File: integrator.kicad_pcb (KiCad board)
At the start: 2 copper layers, 60 x 72 mm, 13 parts, among them J1 SJ-3524-SMT, J2 SJ-3524-SMT, SW1 EVQP40B3M, SW2 EVQP40B3M, U1 Teensy3.2, U2 FXOS8700CQ

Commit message: snapshot everything for safety
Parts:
- added C4: 4.7uf, Capacitor_SMD:CP_Elec_5x4.5, B.Cu at (36.0, 129.9)
- added C5: 0.1uf, Capacitor_SMD:C_0805_2012Metric, B.Cu at (57.6, 26.8)
- added C6: 4.7uf, Capacitor_SMD:CP_Elec_5x4.5, B.Cu at (83.5, 129.9)
- added D1: SD0805S020S1R0, Diode_SMD:D_0805_2012Metric, B.Cu at (49.9, 36.4)
- added R2: 4.7k, Resistor_SMD:R_0805_2012Metric, B.Cu at (49.3, 117.3)
- added R3: 4.7k, Resistor_SMD:R_0805_2012Metric, B.Cu at (49.3, 112.2)
- added R4: 5k, Resistor_SMD:R_0805_2012Metric, B.Cu at (37.2, 32.8)
- added R5: 5k, Resistor_SMD:R_0805_2012Metric, B.Cu at (80.7, 32.8)
- added R6: 4.7k, Resistor_SMD:R_0805_2012Metric, B.Cu at (69.8, 36.6)
- added REF**: hackzone, export:hackzone, B.Cu at (59.7, 82.7)
- C1: value 0.1uF -> 10nf; footprint Capacitor_SMD:C_0603_1608Metric -> Capacitor_SMD:C_0805_2012Metric; moved to B.Cu
- C2: value 0.1uF -> 0.1uf; footprint Capacitor_SMD:C_0603_1608Metric -> Capacitor_SMD:C_0805_2012Metric; moved to B.Cu
- C3: value 0.1uF -> 2.2uf; footprint Capacitor_SMD:C_0603_1608Metric -> Capacitor_SMD:C_0805_2012Metric; moved to B.Cu
- J1, J2: moved to B.Cu
- LED1, LED2: footprint LED_SMD:LED_0603_1608Metric -> LED_SMD:LED_0805_2012Metric; moved to B.Cu
- POGO1: value Conn_02x06_Odd_Even_MountingPin -> PO pogos; footprint Connector_PinSocket_2.54mm:PinSocket_2x06_P2.54mm_Vertical -> export:813-22-012-30-004101-millmax-pogopins-2x6
- R1: footprint Resistor_SMD:R_0603_1608Metric -> Resistor_SMD:R_0805_2012Metric; moved to B.Cu
- SW1: footprint eec:Panasonic-EVQP40B3M-MFG-2pad -> Button_Switch_THT:TL1105VF100Q; moved to B.Cu
- SW2: footprint eec:Panasonic-EVQP40B3M-MFG-2pad -> export:TL1105VF100Q; moved to B.Cu
- U2: value FXOS8700CQ -> ICM-20600; footprint misc:FSOS8700CQ_PKG -> PQFN50P250X300X97-14N; moved to B.Cu
- moved U1 122.8 mm to (59.8, 117.2), turned to 90 degrees
- moved SW1 122.6 mm to (85.5, 47.9), turned to 270 degrees
- moved LED2 119.0 mm to (69.6, 20.0), turned to 0 degrees
- moved J2 116.9 mm to (83.2, 24.6)
- moved R1 116.7 mm to (60.2, 19.9), turned to 90 degrees
- moved J1 115.8 mm to (36.3, 24.6)
- moved LED1 115.1 mm to (50.0, 20.0), turned to 180 degrees
- moved SW2 112.8 mm to (34.0, 47.8), turned to 90 degrees
- moved U2 110.2 mm to (60.2, 23.9), turned to 270 degrees
- moved POGO1 109.4 mm to (59.7, 36.5), turned to 180 degrees
- moved C3 108.2 mm to (63.9, 26.7), turned to 0 degrees
- moved C2 106.0 mm to (63.9, 29.0)
- moved C1 104.9 mm to (63.9, 23.2), turned to 180 degrees
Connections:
- C1 pad 1: Net-(C1-Pad1) -> Earth
- C1 pad 2: Earth -> Net-(C1-Pad2)
- C2 pad 1: Net-(C2-Pad1) -> Net-(C1-Pad2)
- C3 pad 1: Net-(C3-Pad1) -> Net-(C1-Pad2)
- J1 pad 1: Earth -> Net-(J1-Pad1)
- J2 pad 1: Earth -> Net-(J1-Pad1)
- POGO1 pad 4: Net-(POGO1-Pad4) -> Net-(D1-Pad2)
- SW2 pad 1: Earth -> Net-(SW2-Pad1)
- SW2 pad 2: Net-(SW2-Pad2) -> Earth
- U1 pad 11: Net-(SW2-Pad2) -> Net-(SW2-Pad1)
- U1 pad 13: Net-(U1-Pad13) -> Net-(J1-Pad2)
- U1 pad 16: Net-(C1-Pad1) -> Net-(U1-Pad16)
- U1 pad 19: Net-(J2-Pad3) -> Net-(R4-Pad1)
- U1 pad 25: Net-(U1-Pad25) -> Net-(R3-Pad2)
- U1 pad 26: Net-(U1-Pad26) -> Net-(R2-Pad2)
- U1 pad 31: Net-(U1-Pad31) -> Net-(C1-Pad2)
- U1 pad 32: Net-(U1-Pad32) -> Net-(J1-Pad1)
- U1 pad 33: Net-(POGO1-Pad4) -> Net-(U1-Pad33)
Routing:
- net Net-(C1-Pad2): track 0.00 -> 290.7 mm, vias 0 -> 8
- net Net-(J1-Pad1): track 0.00 -> 142.1 mm, vias 0 -> 2
- net (no net): track 0.00 -> 124.5 mm
- net Net-(POGO1-Pad4): track 86.2 -> 0.00 mm, vias 1 -> 0
- net Net-(R4-Pad1): track 0.00 -> 85.7 mm, vias 0 -> 2
- net Net-(POGO1-Pad5): track 85.5 -> 0.00 mm, vias 1 -> 0
- net Net-(POGO1-Pad7): track 82.5 -> 0.00 mm, vias 1 -> 0
- net Net-(POGO1-Pad9): track 79.7 -> 0.00 mm, vias 1 -> 0
- net Net-(J2-Pad3): track 94.3 -> 16.8 mm, vias 3 -> 0
- net Net-(J1-Pad2): track 0.00 -> 76.8 mm, vias 0 -> 1
- net Net-(POGO1-Pad12): track 106.1 -> 34.9 mm, vias 3 -> 0
- net Net-(POGO1-Pad3): track 85.4 -> 19.5 mm, vias 0 -> 2
- net Earth: track 97.6 -> 34.2 mm, vias 6 -> 16
- net Net-(J2-Pad2): track 92.8 -> 47.5 mm, vias 2 -> 1
- net Net-(U1-Pad4): track 44.0 -> 3.34 mm, vias 2 -> 1
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- added copper zone on In1.Cu, net Earth
- added copper zone on In2.Cu, net Earth
- added copper zone on In1.Cu, net Net-(J1-Pad1)
- removed copper zone on F.Cu, net Earth
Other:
- board size 60 x 72 mm -> 65.5 x 217 mm
- copper layers 2 -> 4
- net class +3.3v removed
- net class +v supply added: clearance 0.1524, trace_width 0.5, via_dia 0.6858, via_drill 0.3302
- net class audio added: clearance 0.1524, trace_width 0.5, via_dia 0.6858, via_drill 0.3302
- rule trace_min: 0.1524 -> 0.127

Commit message: snapshot with hackzone
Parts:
- moved D1 72.1 mm to (46.0, 108.3)
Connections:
- U1 pad 2: Net-(U1-Pad2) -> Net-(SW1-Pad2)
- U1 pad 5: Net-(SW1-Pad2) -> Net-(U1-Pad5)
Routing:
- net Net-(J1-Pad1): track 142.1 -> 312.8 mm
- net Net-(R3-Pad2): track 11.5 -> 121.7 mm
- net Net-(POGO1-Pad6): track 54.7 -> 160.0 mm
- net Net-(U1-Pad3): track 4.66 -> 105.9 mm, vias 1 -> 0
- net Net-(POGO1-Pad5): track 0.00 -> 95.7 mm
- net Net-(LED2-Pad2): track 67.3 -> 155.7 mm
- net Net-(D1-Pad2): track 9.50 -> 96.5 mm, vias 0 -> 2
- net Net-(R2-Pad2): track 11.8 -> 93.0 mm
- net Net-(SW1-Pad2): track 20.1 -> 90.4 mm
- net Net-(LED1-Pad2): track 68.3 -> 130.3 mm
- net Net-(POGO1-Pad12): track 34.9 -> 96.4 mm
- net Net-(U1-Pad4): track 3.34 -> 60.9 mm, vias 1 -> 0
- net Net-(R4-Pad1): track 85.7 -> 142.1 mm
- net Net-(POGO1-Pad9): track 0.00 -> 54.0 mm
- net Net-(POGO1-Pad7): track 0.00 -> 52.2 mm
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
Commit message: bye bye hackzone
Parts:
- removed REF**: hackzone, export:hackzone
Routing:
- net (no net): track 124.5 -> 0.00 mm
- net Net-(R2-Pad2): track 93.0 -> 127.2 mm, vias 1 -> 3
- net Net-(C1-Pad2): track 290.2 -> 268.1 mm
- net Net-(J1-Pad1): track 312.8 -> 332.8 mm, vias 2 -> 4
- net Net-(SW1-Pad2): track 90.4 -> 103.2 mm
- net Net-(J2-Pad2): track 96.7 -> 107.4 mm
- net Net-(LED2-Pad2): track 155.7 -> 166.2 mm, vias 0 -> 2
- net Net-(J1-Pad2): track 124.1 -> 134.2 mm
- net Net-(R4-Pad1): track 142.1 -> 150.4 mm
- net Net-(LED1-Pad2): track 130.3 -> 137.0 mm
- net Net-(R3-Pad2): track 121.7 -> 127.8 mm

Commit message: last changes of rev3
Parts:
- added REF**: PinSocket_2x02_P2.54mm_Vertical, Connector_PinSocket_2.54mm:PinSocket_2x02_P2.54mm_Vertical, F.Cu at (136.6, 133.0)
- moved C3 98.2 mm to (158.4, 53.5), turned to 270 degrees
- moved R2 97.8 mm to (143.6, 143.3)
- moved C4 97.8 mm to (130.3, 155.9)
- moved C6 97.8 mm to (177.8, 155.9)
- moved POGO1 97.8 mm to (154.0, 62.5)
- moved R3 97.8 mm to (143.6, 138.2)
- moved R6 97.8 mm to (164.2, 62.6)
- moved SW1 97.8 mm to (179.8, 73.9)
- moved SW2 97.8 mm to (128.3, 73.8)
- moved U1 97.8 mm to (154.1, 143.2)
- moved U2 97.8 mm to (154.5, 49.9)
- moved D1 97.8 mm to (140.3, 134.3)
- moved J1 97.8 mm to (130.6, 50.6)
- moved J2 97.8 mm to (177.5, 50.6)
- moved LED1 97.8 mm to (144.3, 46.0)
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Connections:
- net Net-(C1-Pad2) renamed /+3.3v
- net Net-(D1-Pad2) renamed /po_batt
- net Net-(J1-Pad1) renamed /a_gnd
- net Net-(J1-Pad2) renamed /l_sync_out
- net Net-(J2-Pad2) renamed /r_sync_out
- net Net-(LED1-Pad2) renamed /led1
- net Net-(LED2-Pad2) renamed /led2
- net Net-(POGO1-Pad12) renamed /po_play
- net Net-(POGO1-Pad3) renamed /po_reset
- net Net-(POGO1-Pad5) renamed /swclk
- net Net-(POGO1-Pad6) renamed /po_wake
- net Net-(POGO1-Pad7) renamed /swdio
- net Net-(POGO1-Pad9) renamed /swo
- net Net-(R2-Pad2) renamed /i2c_clk
- net Net-(R3-Pad2) renamed /i2c_sda
- net Net-(R4-Pad1) renamed /dac
- net Net-(SW1-Pad2) renamed /l_button
- net Net-(SW2-Pad1) renamed /r_button
- net Net-(U1-Pad3) renamed /amu_sync
- net Net-(U1-Pad4) renamed /amu_int2
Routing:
- net /po_reset: track 57.3 -> 185.6 mm, vias 3 -> 5
- net /amu_int2: track 60.9 -> 158.1 mm, vias 0 -> 2
- net /swo: track 54.0 -> 147.2 mm, vias 0 -> 2
- net /swdio: track 52.2 -> 137.5 mm, vias 0 -> 2
- net /amu_sync: track 105.9 -> 163.6 mm, vias 0 -> 2
- net /a_gnd: track 332.8 -> 275.8 mm
- net /r_button: track 39.9 -> 91.5 mm, vias 0 -> 2
- net /po_play: track 96.4 -> 142.4 mm, vias 0 -> 2
- net /swclk: track 95.7 -> 135.0 mm, vias 0 -> 2
- net Earth: track 34.3 -> 61.4 mm, vias 16 -> 18
- net /+3.3v: track 268.1 -> 285.0 mm
- net /led2: track 166.2 -> 179.3 mm
- net /po_batt: track 96.5 -> 103.9 mm
- net /po_wake: track 160.1 -> 165.6 mm
- net /i2c_clk: track 127.2 -> 132.3 mm
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- added copper zone on B.Cu, net Earth
- added copper zone on F.Cu, net Earth
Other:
- board size 65.5 x 217 mm -> 65.5 x 117 mm
- net class Default: clearance 0.1524 -> 0.1523
- rule trace_clearance: 0.1524 -> 0.1523
- board text added: "MSL Pocket Integrator rev1 Spring 2021"
- board text added: "magic fingers"
- board text added: "• attach with bolts, glue or duct tape • connect either output to PO input • set PO sync mode to SY4 • unplug to let PO sleep • repetition is a form of change"
- board text removed: "MSL"

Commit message: evt4 pcb layout
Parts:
- removed C5: 0.1uf, Capacitor_SMD:C_0805_2012Metric
- removed R3: 4.7k, Resistor_SMD:R_0805_2012Metric
- removed U2: ICM-20600, PQFN50P250X300X97-14N
- added IMU: ICM-42605, ICM-42605:PQFN50P300X250X97-14N, B.Cu at (154.0, 95.3)
- added NON       STOP: SW_Push_LED, TL3215AF160BQ:E-Switch-N326000-0-0-0, B.Cu at (154.0, 50.6)
- D1: footprint Diode_SMD:D_0805_2012Metric -> Diode_SMD:D_SOD-323
- R2: value 4.7k -> 47
- moved R2 98.5 mm to (164.3, 47.0), turned to 180 degrees
- moved C1 47.0 mm to (150.8, 95.6), turned to 90 degrees
- moved C2 41.9 mm to (157.1, 95.4)
- moved C3 41.9 mm to (159.4, 95.4)
- moved R6 18.8 mm to (145.3, 62.5)
- moved LED1 18.0 mm to (126.3, 46.2), turned to 225 degrees
- moved LED2 17.8 mm to (181.7, 46.1), turned to 315 degrees
- moved SW2 14.8 mm to (128.3, 88.5)
- moved SW1 14.6 mm to (179.8, 88.5)
- moved R1 11.7 mm to (143.0, 47.6), turned to 270 degrees
- moved D1 8.42 mm to (139.8, 142.7)
- moved REF** 8.42 mm to (136.1, 141.4)
- moved R4 5.90 mm to (135.7, 54.7), turned to 180 degrees
- moved R5 4.19 mm to (174.2, 54.6), turned to 180 degrees
- renumbered C6 to DUM, C4 to DUM_R
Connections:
- POGO1 pad 10: Net-(POGO1-Pad10) -> Earth
- POGO1 pad 11: Net-(POGO1-Pad11) -> /po_batt
- POGO1 pad 2: Earth -> Net-(POGO1-Pad2)
- POGO1 pad 4: /po_batt -> Net-(POGO1-Pad4)
- R2 pad 1: /+3.3v -> Earth
- R2 pad 2: /i2c_clk -> Net-(R2-Pad2)
- R6 pad 1: Net-(POGO1-Pad11) -> /po_reset
- R6 pad 2: /po_reset -> Earth
- REF** pad 1: (no net) -> Earth
- SW1 pad 2: /l_button -> /sw1
- SW2 pad 1: /r_button -> /sw2
- U1 pad 10: /r_sync_out -> /led2
- U1 pad 11: /r_button -> /po_wake
- U1 pad 12: Net-(U1-Pad12) -> /spi_cs
- U1 pad 13: /l_sync_out -> /spi_mosi
- U1 pad 14: Net-(U1-Pad14) -> /spi_miso
- U1 pad 2: /l_button -> /nonstop_sw
- U1 pad 20: Net-(U1-Pad20) -> /spi_clock
- U1 pad 22: Net-(U1-Pad22) -> /led1
- U1 pad 24: /po_wake -> Net-(U1-Pad24)
- U1 pad 25: /i2c_sda -> Net-(U1-Pad25)
- U1 pad 26: /i2c_clk -> Net-(U1-Pad26)
- U1 pad 27: /led1 -> /l_sync_out
- U1 pad 28: /led2 -> /sw1
- U1 pad 29: Net-(U1-Pad29) -> /sw2
- U1 pad 3: /amu_sync -> /nonstop_led
- U1 pad 30: Net-(U1-Pad30) -> /r_sync_out
- U1 pad 4: /amu_int2 -> /imu_int1
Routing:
- net /a_gnd: track 275.8 -> 4.28 mm, vias 4 -> 3
- net /amu_sync: track 163.6 -> 0.00 mm, vias 2 -> 0
- net /amu_int2: track 158.1 -> 0.00 mm, vias 2 -> 0
- net /nonstop_sw: track 0.00 -> 153.2 mm
- net /nonstop_led: track 0.00 -> 149.0 mm, vias 0 -> 2
- net /+3.3v: track 285.0 -> 148.6 mm, vias 7 -> 4
- net /i2c_clk: track 132.3 -> 0.00 mm, vias 3 -> 0
- net /i2c_sda: track 131.2 -> 0.00 mm, vias 1 -> 0
- net /sw1: track 0.00 -> 106.8 mm, vias 0 -> 2
- net /l_button: track 105.1 -> 0.00 mm
- net /r_button: track 91.5 -> 0.00 mm, vias 2 -> 0
- net /led2: track 179.3 -> 101.1 mm
- net /sw2: track 0.00 -> 73.8 mm
- net /imu_int1: track 0.00 -> 73.8 mm, vias 0 -> 2
- net /po_wake: track 165.6 -> 104.7 mm, vias 0 -> 2
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- added copper zone on In2.Cu, net /+3.3v
- added copper zone on F.Cu, net /a_gnd
- removed copper zone on In2.Cu, net Earth
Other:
- outline, holes or cut-outs redrawn
- board text added: "+bat"
- board text added: "+usb"
- board text added: "F_U_CN_RD UR_BKWDS"
- board text added: "MSL Pocket Integrator evt4 Summer 2021"
- board text added: "NON STOP"
- board text added: "OUT"
- board text added: "PO INPUT"
- board text added: "TO WORLD"
- board text added: "clock"
- board text added: "cs"
- board text added: "gnd-"
- board text added: "miso"
- board text added: "mosi"
- board text added: "silicone O ring: 1.75”/44mm inside diameter"
- board text added: "• attach with 2 O rings 1.75”/44mm I.D. • connect either output to PO input • set PO sync mode to SY4 • shake it like a polaroid picture"
- board text removed: "MSL Pocket Integrator rev1 Spring 2021"
- board text removed: "• attach with bolts, glue or duct tape • connect either output to PO input • set PO sync mode to SY4 • unplug to let PO sleep • repetition is a form of change"

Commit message: even more final evt4
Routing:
- net /dac: track 138.4 -> 143.2 mm
- net /l_sync_out: track 162.7 -> 167.4 mm
- net /r_sync_out: track 136.2 -> 138.7 mm
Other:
- board text added: "n/c"
- board text added: "• attach with two O rings 1.75”/44mm I.D. • connect either output to PO input • set PO sync mode to SY4 • shake it like a polaroid picture"
- board text removed: "clock"
- board text removed: "cs"
- board text removed: "miso"
- board text removed: "mosi"
- board text removed: "• attach with 2 O rings 1.75”/44mm I.D. • connect either output to PO input • set PO sync mode to SY4 • shake it like a polaroid picture"

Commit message: evt4 submitted to oshpark
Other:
- board text added: "• attach with two O rings 1.75”/44mm I.D. • connect either out to PO input • set PO sync mode to SY4 • shake it like a polaroid picture"
- board text removed: "• attach with two O rings 1.75”/44mm I.D. • connect either output to PO input • set PO sync mode to SY4 • shake it like a polaroid picture"

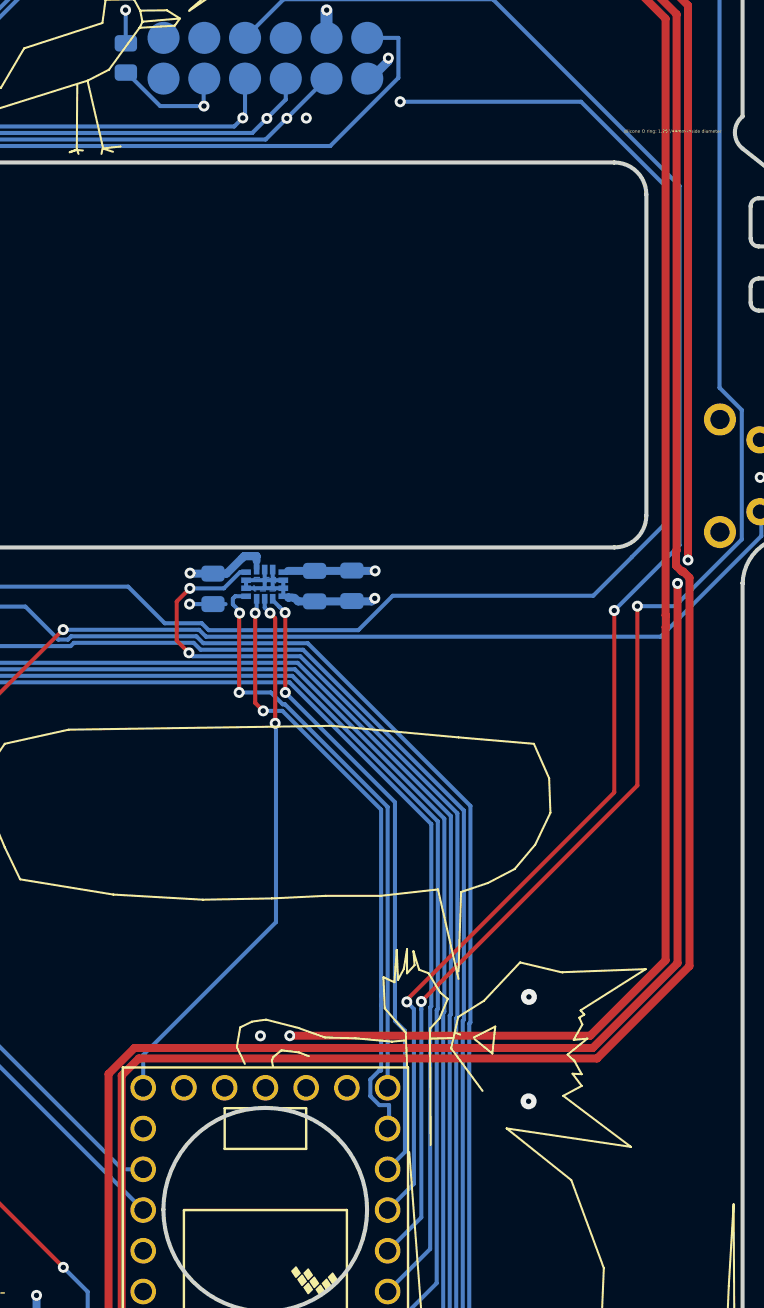
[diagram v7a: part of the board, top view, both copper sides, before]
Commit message: moved po_wake to analog pin 14 +tweaks
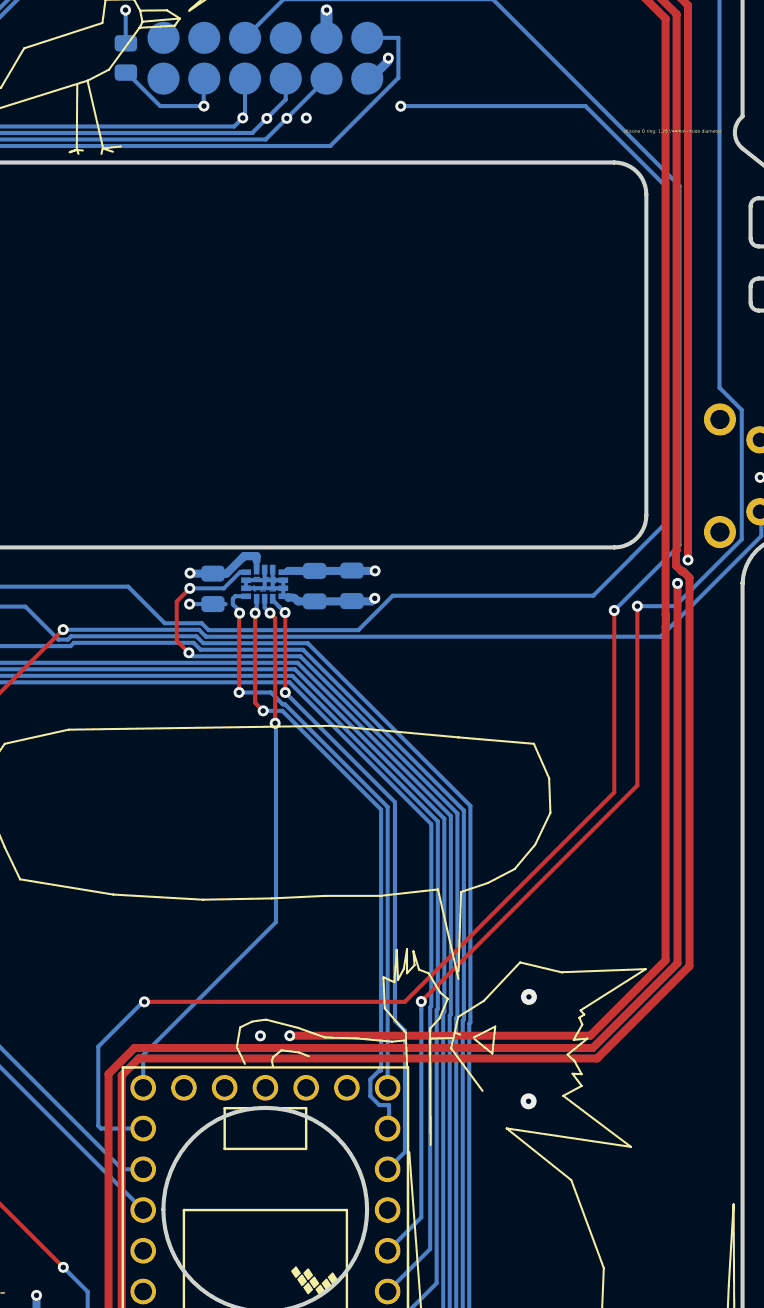
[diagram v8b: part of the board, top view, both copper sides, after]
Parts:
- SW3: renamed from NON       STOP
- renumbered DUM_R to C4, DUM to C6, IMU to U2
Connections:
- U1 pad 11: /po_wake -> Net-(U1-Pad11)
- U1 pad 21: Net-(U1-Pad21) -> /po_wake
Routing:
- net /po_wake: track 104.7 -> 119.0 mm
- net /po_reset: track 184.8 -> 183.5 mm
